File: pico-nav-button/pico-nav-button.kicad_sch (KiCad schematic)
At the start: 4 parts, among them J1 Conn_01x04, J2 Conn_01x04, U1 Nav_Button, U2 Slider

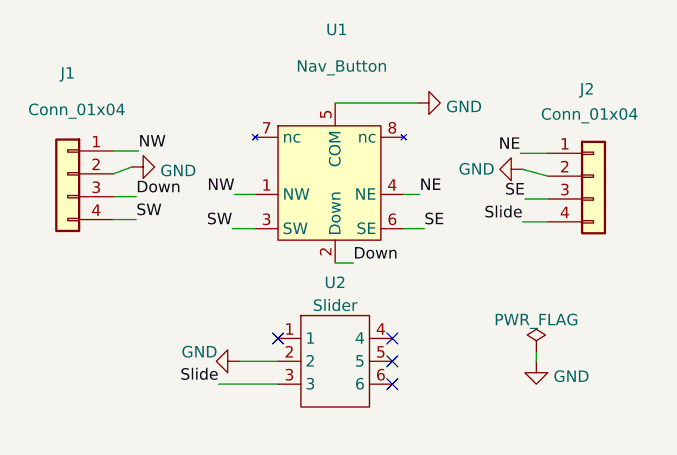
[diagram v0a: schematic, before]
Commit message: Rev 1.10: fixed pad-to-pin assignments
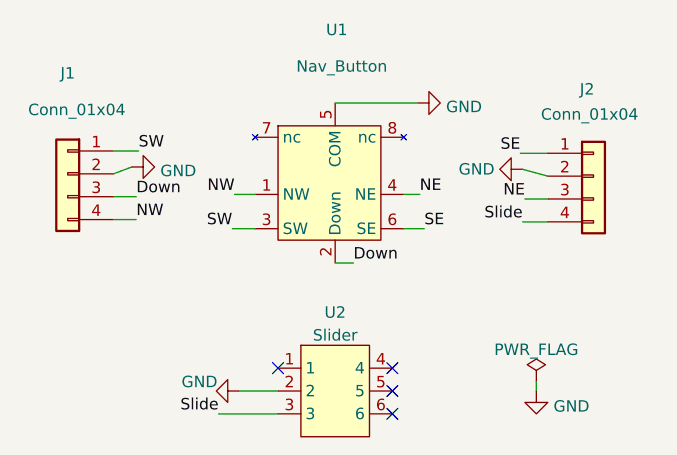
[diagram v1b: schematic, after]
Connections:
- net NE: now also J2.3 (Pin_3); no longer J2.1 (Pin_1)
- net NW: now also J1.4 (Pin_4); no longer J1.1 (Pin_1)
- net SE: now also J2.1 (Pin_1); no longer J2.3 (Pin_3)
- net SW: now also J1.1 (Pin_1); no longer J1.4 (Pin_4)
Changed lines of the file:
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@@
   (title_block
     (title "Pico Navigation Button")
-    (date "2024-04-02")
-    (rev "0.1")
+    (date "2024-04-24")
+    (rev "1.10")
     (company "Bernhard Bablok")
     (comment 1 "https://github.com/bablokb/pcb-pico-nav-button")
   )
-  (no_connect (at 117.602 66.548))
-  (no_connect (at 117.602 71.628))
-  (no_connect (at 117.602 69.088))
-  (no_connect (at 104.902 66.548))
+  (no_connect (at 117.602 69.85))
+  (no_connect (at 117.602 74.93))
+  (no_connect (at 117.602 72.39))
+  (no_connect (at 104.902 69.85))
   (wire (pts (xy 131.826 45.974) (xy 134.874 45.974))
     (stroke (width 0) (type default) (color 0 0 0 0))
@@
     (stroke (width 0) (type default) (color 0 0 0 0))
   )
-  (wire (pts (xy 133.604 69.088) (xy 133.604 68.072))
+  (wire (pts (xy 133.604 72.39) (xy 133.604 71.374))
     (stroke (width 0) (type default) (color 0 0 0 0))
   )
@@
     (stroke (width 0) (type default) (color 0 0 0 0))
   )
-  (wire (pts (xy 100.584 69.088) (xy 104.902 69.088))
+  (wire (pts (xy 100.584 72.39) (xy 104.902 72.39))
     (stroke (width 0) (type default) (color 0 0 0 0))
   )
@@
     (stroke (width 0) (type default) (color 0 0 0 0))
   )
-  (wire (pts (xy 98.298 71.628) (xy 104.902 71.628))
+  (wire (pts (xy 98.298 74.93) (xy 104.902 74.93))
     (stroke (width 0) (type default) (color 0 0 0 0))
   )
@@
     (effects (font (size 1.27 1.27)) (justify left bottom))
   )
-  (label "NW" (at 89.408 45.72 0)
+  (label "NW" (at 89.154 53.34 0)
     (effects (font (size 1.27 1.27)) (justify left bottom))
   )
@@
     (effects (font (size 1.27 1.27)) (justify left bottom))
   )
-  (label "NE" (at 131.826 45.974 180)
+  (label "NE" (at 132.334 51.054 180)
     (effects (font (size 1.27 1.27)) (justify right bottom))
   )
-  (label "Slide" (at 98.298 71.628 180)
+  (label "Slide" (at 98.298 74.93 180)
     (effects (font (size 1.27 1.27)) (justify right bottom))
   )
@@
     (effects (font (size 1.27 1.27)) (justify right bottom))
   )
-  (label "SW" (at 89.154 53.34 0)
+  (label "SW" (at 89.408 45.72 0)
     (effects (font (size 1.27 1.27)) (justify left bottom))
   )
@@
     (effects (font (size 1.27 1.27)) (justify right bottom))
   )
-  (label "SE" (at 132.334 51.054 180)
+  (label "SE" (at 131.826 45.974 180)
     (effects (font (size 1.27 1.27)) (justify right bottom))
   )
@@
     (effects (font (size 1.27 1.27)) (justify left bottom))
   )
-  (symbol (lib_id "power:GND") (at 133.604 69.088 0) (unit 1)
+  (symbol (lib_id "power:GND") (at 133.604 72.39 0) (unit 1)
     (in_bom yes) (on_board yes) (fields_autoplaced)
-    (property "Reference" "#PWR0102" (id 0) (at 133.604 75.438 0)
+    (property "Reference" "#PWR0102" (id 0) (at 133.604 78.74 0)
       (effects (font (size 1.27 1.27)) hide)
     )
-    (property "Value" "GND" (id 1) (at 135.509 70.7918 0)
+    (property "Value" "GND" (id 1) (at 135.509 74.0938 0)
       (effects (font (size 1.27 1.27)) (justify left))
     )
-    (property "Footprint" "" (id 2) (at 133.604 69.088 0)
+    (property "Footprint" "" (id 2) (at 133.604 72.39 0)
       (effects (font (size 1.27 1.27)) hide)
     )
-    (property "Datasheet" "" (id 3) (at 133.604 69.088 0)
+    (property "Datasheet" "" (id 3) (at 133.604 72.39 0)
       (effects (font (size 1.27 1.27)) hide)
     )
     (pin "1")
   )
-  (symbol (lib_id "power:PWR_FLAG") (at 133.604 68.072 0) (unit 1)
+  (symbol (lib_id "power:PWR_FLAG") (at 133.604 71.374 0) (unit 1)
     (in_bom yes) (on_board yes) (fields_autoplaced)
-    (property "Reference" "#FLG0101" (id 0) (at 133.604 66.167 0)
+    (property "Reference" "#FLG0101" (id 0) (at 133.604 69.469 0)
       (effects (font (size 1.27 1.27)) hide)
     )
-    (property "Value" "PWR_FLAG" (id 1) (at 133.604 64.4962 0))
-    (property "Footprint" "" (id 2) (at 133.604 68.072 0)
+    (property "Value" "PWR_FLAG" (id 1) (at 133.604 67.7982 0))
+    (property "Footprint" "" (id 2) (at 133.604 71.374 0)
       (effects (font (size 1.27 1.27)) hide)
     )
-    (property "Datasheet" "~" (id 3) (at 133.604 68.072 0)
+    (property "Datasheet" "~" (id 3) (at 133.604 71.374 0)
       (effects (font (size 1.27 1.27)) hide)
     )
@@
     (pin "8")
   )
-  (symbol (lib_id "power:GND") (at 100.584 69.088 270) (unit 1)
+  (symbol (lib_id "power:GND") (at 100.584 72.39 270) (unit 1)
     (in_bom yes) (on_board yes)
-    (property "Reference" "#PWR01" (id 0) (at 94.234 69.088 0)
+    (property "Reference" "#PWR01" (id 0) (at 94.234 72.39 0)
       (effects (font (size 1.27 1.27)) hide)
     )
-    (property "Value" "GND" (id 1) (at 98.171 68.072 90)
+    (property "Value" "GND" (id 1) (at 98.171 71.374 90)
       (effects (font (size 1.27 1.27)) (justify right))
     )
-    (property "Footprint" "" (id 2) (at 100.584 69.088 0)
+    (property "Footprint" "" (id 2) (at 100.584 72.39 0)
       (effects (font (size 1.27 1.27)) hide)
     )
-    (property "Datasheet" "" (id 3) (at 100.584 69.088 0)
+    (property "Datasheet" "" (id 3) (at 100.584 72.39 0)
       (effects (font (size 1.27 1.27)) hide)
     )
     (pin "1")
   )
-  (symbol (lib_id "user:Slider") (at 111.252 69.088 0) (unit 1)
+  (symbol (lib_id "user:Slider") (at 111.252 72.39 0) (unit 1)
     (in_bom yes) (on_board yes) (fields_autoplaced)
-    (property "Reference" "U2" (id 0) (at 111.252 60.359 0))
-    (property "Value" "Slider" (id 1) (at 111.252 62.8959 0))
-    (property "Footprint" "user:Slider" (id 2) (at 111.252 79.248 0)
+    (property "Reference" "U2" (id 0) (at 111.252 63.661 0))
+    (property "Value" "Slider" (id 1) (at 111.252 66.1979 0))
+    (property "Footprint" "user:Slider" (id 2) (at 111.252 82.55 0)
       (effects (font (size 1.27 1.27)) hide)
     )
-    (property "Datasheet" "" (id 3) (at 104.902 66.548 0)
+    (property "Datasheet" "" (id 3) (at 104.902 69.85 0)
       (effects (font (size 1.27 1.27)) hide)
     )
-    (property "LCSC" "C381098" (id 4) (at 111.252 69.088 0)
+    (property "LCSC" "C381098" (id 4) (at 111.252 72.39 0)
       (effects (font (size 1.27 1.27)) hide)
     )
